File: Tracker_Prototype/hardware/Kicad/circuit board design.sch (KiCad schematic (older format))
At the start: 30 parts, among them J1 Conn_01x06, J2 GND, J3 3.3V, J4 Unconnected, U1 MAX-M8C, U3 CMWX1ZZABZ-078, U6 MS5607-02BA

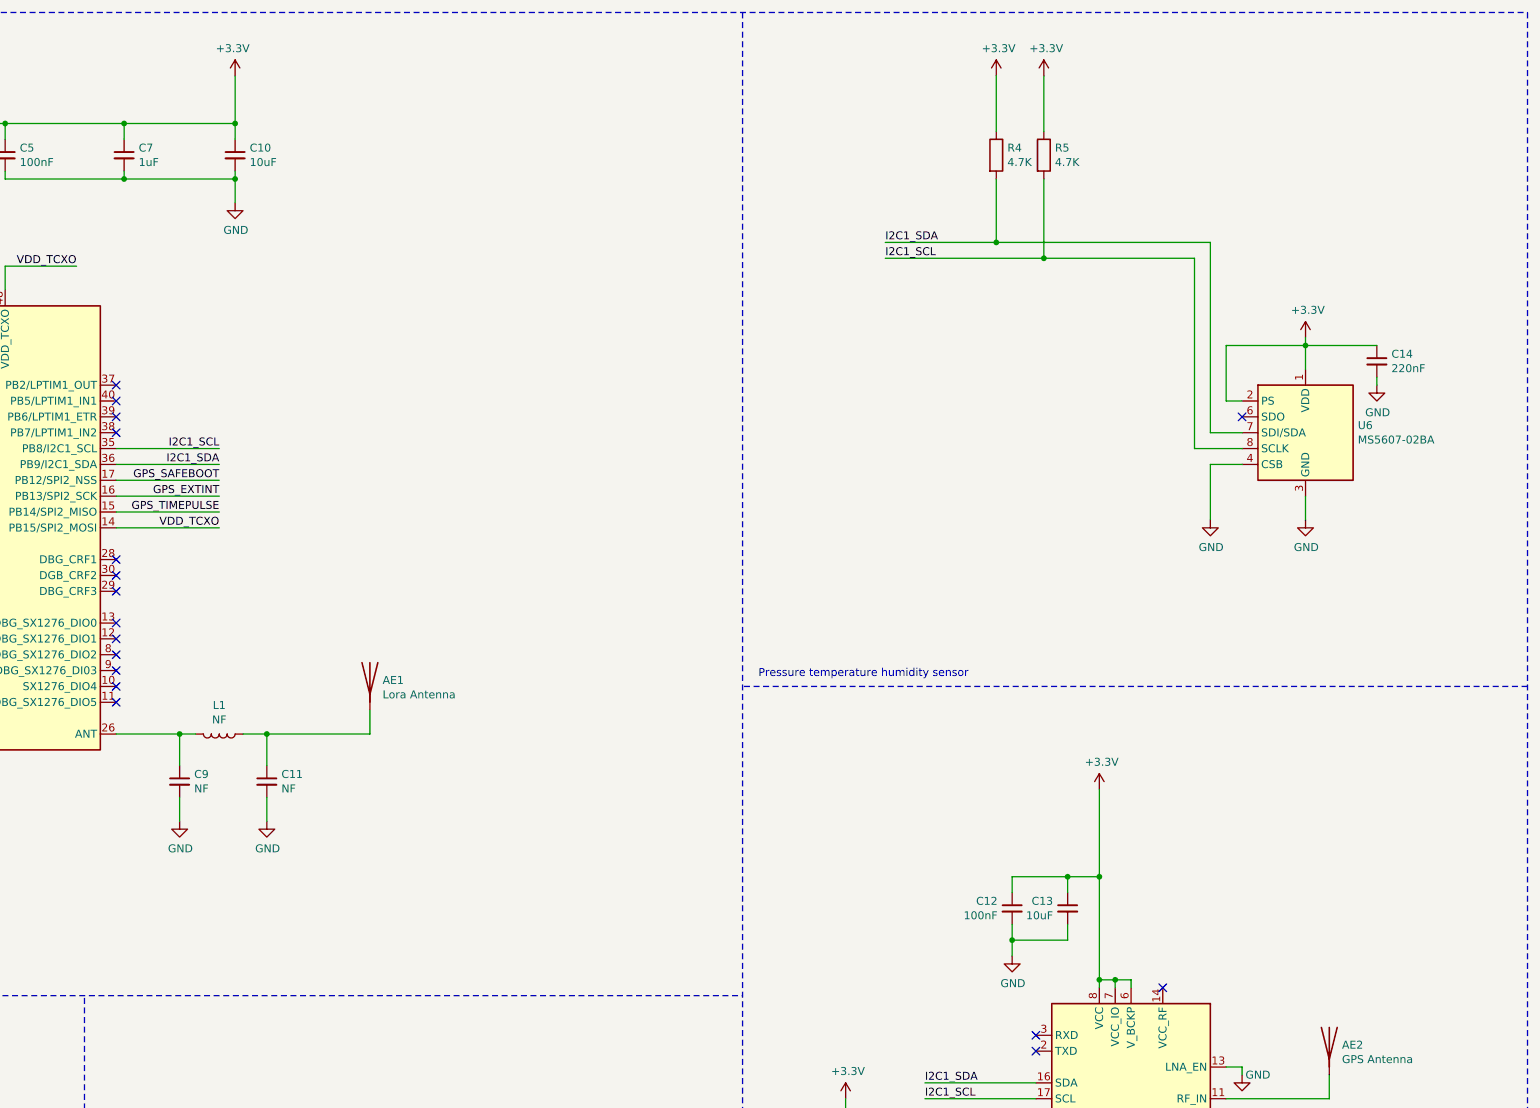
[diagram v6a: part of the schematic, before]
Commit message: added in indicator LED, added in push button to circuit only.
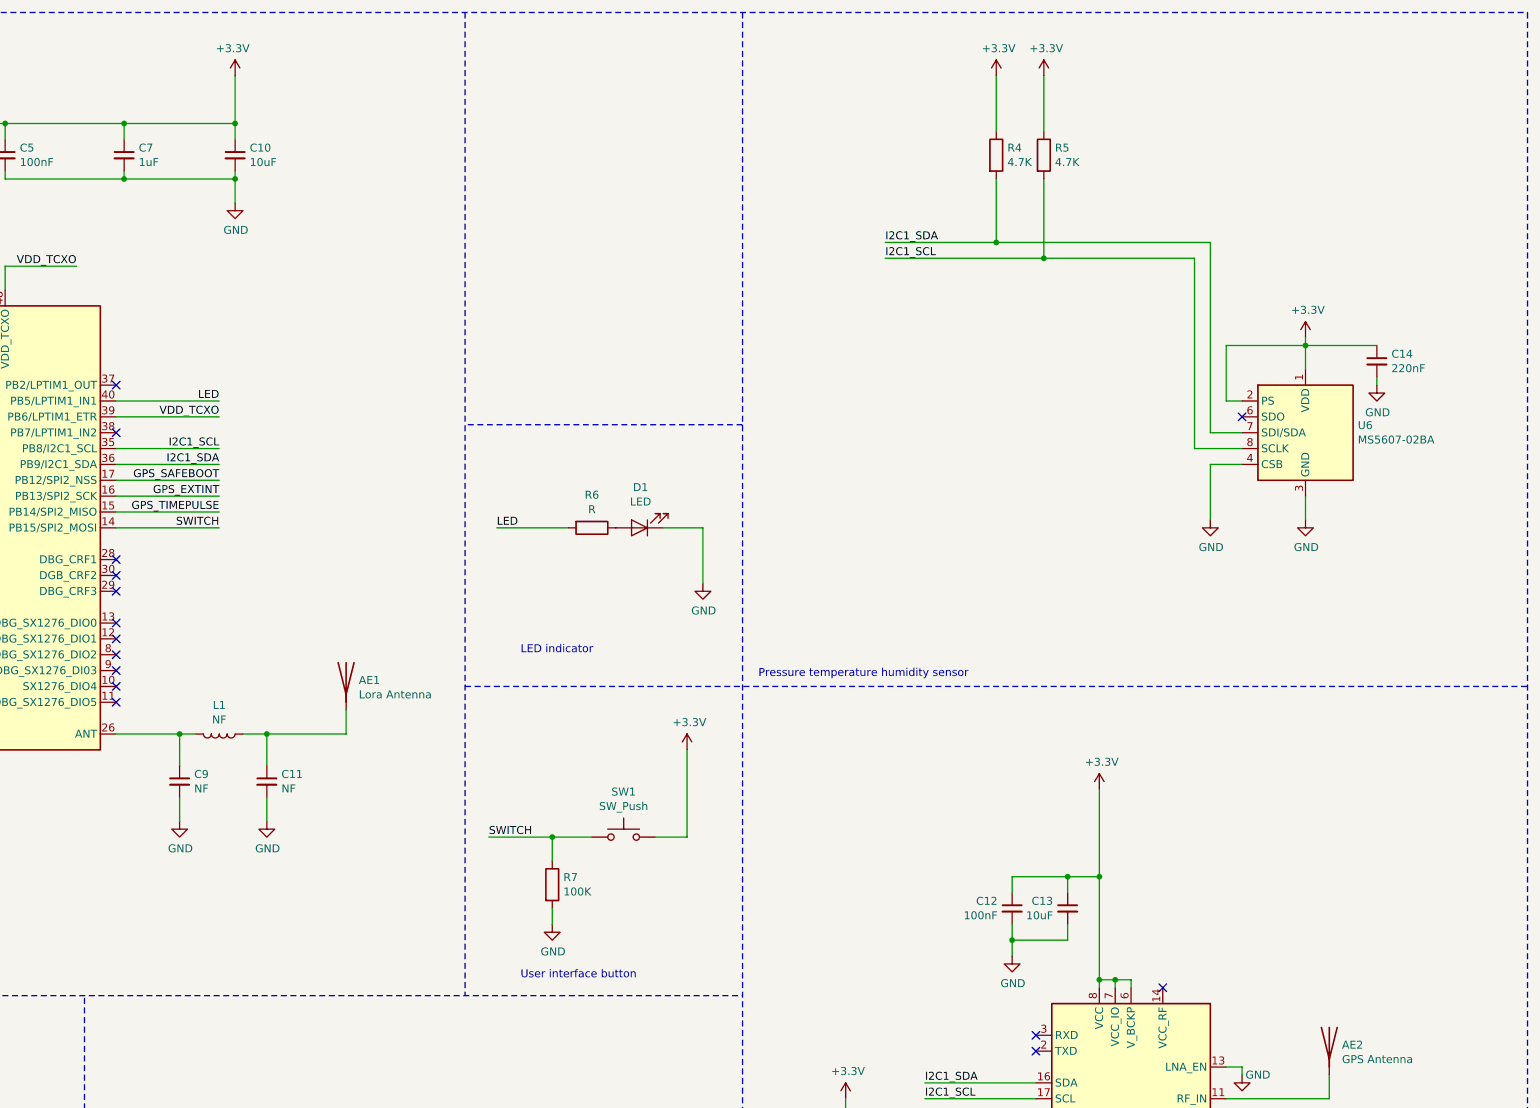
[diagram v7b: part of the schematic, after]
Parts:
- added D1: LED, LED_SMD:LED_0402_1005Metric, symbol Device:LED
- added R6: R, Resistor_SMD:R_0402_1005Metric, symbol Device:R
- added R7: 100K, Resistor_SMD:R_0402_1005Metric, symbol Device:R
- added SW1: SW_Push, symbol Switch:SW_Push
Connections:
- net +3V3: now also SW1.2
- net GND: now also D1.1 (K), R7.2
- net VDD_TCXO: now also U3.39 (PB6/LPTIM1_ETR); no longer U3.14 (PB15/SPI2_MOSI)
- net LED: now reaches U3.40 (PB5/LPTIM1_IN1)
- net LED: now also R6.2
- new net: D1.2 (A), R6.1
- new net SWITCH: R7.1, SW1.1, U3.14 (PB15/SPI2_MOSI)
- no-connect marks 33 -> 31
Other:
- note added: "LED indicator\n"
- note added: "User interface button\n"
- moved on the sheet: AE1
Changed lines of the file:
@@
 Text Notes 11200 4850 0    50   ~ 0
 Pressure temperature humidity sensor\n
-Wire Notes Line
-	16050 4900 11100 4900
 Text Notes 11200 9100 0    50   ~ 0
 GPS circuit\n
@@
 I2C1_SDA
 Wire Wire Line
-	8750 5200 8750 5050
-Wire Wire Line
-	8100 5200 8750 5200
+	8600 5200 8600 5050
+Wire Wire Line
+	8100 5200 8600 5200
 Text Label 12000 2100 0    50   ~ 0
 I2C1_SDA
@@
 GPS_EXTINT
 NoConn ~ 7150 3000
-NoConn ~ 7150 3100
-NoConn ~ 7150 3200
 NoConn ~ 7150 3300
 NoConn ~ 7150 4100
@@
 L Device:Antenna AE1
 U 1 1 5DE442FF
-P 8750 4850
-F 0 "AE1" H 8830 4839 50  0000 L CNN
-F 1 "Lora Antenna" H 8830 4748 50  0000 L CNN
-F 2 "Connector_Wire:SolderWirePad_1x01_Drill0.8mm" H 8750 4850 50  0001 C CNN
-F 3 "~" H 8750 4850 50  0001 C CNN
-	1    8750 4850
+P 8600 4850
+F 0 "AE1" H 8680 4839 50  0000 L CNN
+F 1 "Lora Antenna" H 8680 4748 50  0000 L CNN
+F 2 "Connector_Wire:SolderWirePad_1x01_Drill0.8mm" H 8600 4850 50  0001 C CNN
+F 3 "~" H 8600 4850 50  0001 C CNN
+	1    8600 4850
 	1    0    0    -1
 $EndComp
@@
 Text Label 4900 4000 0    50   ~ 0
 SWDIO
-Text Label 7800 3900 2    50   ~ 0
+Text Label 7800 3200 2    50   ~ 0
 VDD_TCXO
 Wire Wire Line
-	7150 3900 7800 3900
+	7150 3200 7800 3200
 Wire Wire Line
 	6050 1350 6050 2400
@@
 NoConn ~ 8950 7650
 NoConn ~ 5350 3900
+Wire Wire Line
+	7150 3100 7800 3100
+Wire Wire Line
+	10850 3900 10850 4250
+$Comp
+L power:GND #PWR?
+U 1 1 5DBBC44F
+P 10850 4250
+AR Path="/5D5B15F7/5DBBC44F" Ref="#PWR?"  Part="1"
+AR Path="/5DBBC44F" Ref="#PWR02"  Part="1"
+F 0 "#PWR02" H 10850 4000 50  0001 C CNN
+F 1 "GND" H 10855 4077 50  0000 C CNN
+F 2 "" H 10850 4250 50  0001 C CNN
+F 3 "" H 10850 4250 50  0001 C CNN
+	1    10850 4250
+	1    0    0    -1
+$EndComp
+$Comp
+L Device:LED D1
+U 1 1 5DBC4B62
+P 10450 3900
+F 0 "D1" H 10443 3645 50  0000 C CNN
+F 1 "LED" H 10443 3736 50  0000 C CNN
+F 2 "LED_SMD:LED_0402_1005Metric" H 10450 3900 50  0001 C CNN
+F 3 "~" H 10450 3900 50  0001 C CNN
+	1    10450 3900
+	-1   0    0    1
+$EndComp
+Wire Wire Line
+	10600 3900 10850 3900
+$Comp
+L Device:R R6
+U 1 1 5DBC5657
+P 10150 3900
+F 0 "R6" V 9943 3900 50  0000 C CNN
+F 1 "R" V 10034 3900 50  0000 C CNN
+F 2 "Resistor_SMD:R_0402_1005Metric" V 10080 3900 50  0001 C CNN
+F 3 "~" H 10150 3900 50  0001 C CNN
+	1    10150 3900
+	0    1    1    0
+$EndComp
+Wire Wire Line
+	7150 3900 7800 3900
+Text Label 7800 3900 2    50   ~ 0
+SWITCH
+Wire Notes Line
+	9350 4900 16050 4900
+Wire Wire Line
+	10150 5850 9900 5850
+Text Label 9500 5850 0    50   ~ 0
+SWITCH
+Wire Wire Line
+	9900 5850 9900 6000
+Connection ~ 9900 5850
+Wire Wire Line
+	9900 5850 9500 5850
+$Comp
+L power:GND #PWR?
+U 1 1 5DC040B5
+P 9900 6400
+AR Path="/5D5B15F7/5DC040B5" Ref="#PWR?"  Part="1"
+AR Path="/5DC040B5" Ref="#PWR03"  Part="1"
+F 0 "#PWR03" H 9900 6150 50  0001 C CNN
+F 1 "GND" H 9905 6227 50  0000 C CNN
+F 2 "" H 9900 6400 50  0001 C CNN
+F 3 "" H 9900 6400 50  0001 C CNN
+	1    9900 6400
+	1    0    0    -1
+$EndComp
+$Comp
+L Switch:SW_Push SW1
+U 1 1 5DC04C37
+P 10350 5850
+F 0 "SW1" H 10350 6135 50  0000 C CNN
+F 1 "SW_Push" H 10350 6044 50  0000 C CNN
+F 2 "" H 10350 6050 50  0001 C CNN
+F 3 "~" H 10350 6050 50  0001 C CNN
+	1    10350 5850
+	1    0    0    -1
+$EndComp
+Wire Wire Line
+	10550 5850 10750 5850
+$Comp
+L power:+3.3V #PWR?
+U 1 1 5DC0A475
+P 10750 5300
+AR Path="/5D5B165E/5DC0A475" Ref="#PWR?"  Part="1"
+AR Path="/5D5B15F7/5DC0A475" Ref="#PWR?"  Part="1"
+AR Path="/5DC0A475" Ref="#PWR04"  Part="1"
+F 0 "#PWR04" H 10750 5150 50  0001 C CNN
+F 1 "+3.3V" H 10765 5473 50  0000 C CNN
+F 2 "" H 10750 5300 50  0001 C CNN
+F 3 "" H 10750 5300 50  0001 C CNN
+	1    10750 5300
+	1    0    0    -1
+$EndComp
+$Comp
+L Device:R R7
+U 1 1 5DC0F569
+P 9900 6150
+F 0 "R7" H 9970 6196 50  0000 L CNN
+F 1 "100K" H 9970 6105 50  0000 L CNN
+F 2 "Resistor_SMD:R_0402_1005Metric" V 9830 6150 50  0001 C CNN
+F 3 "~" H 9900 6150 50  0001 C CNN
+	1    9900 6150
+	1    0    0    -1
+$EndComp
+Text Notes 9700 6750 0    50   ~ 0
+User interface button\n
+Wire Wire Line
+	9900 6300 9900 6400
+Wire Wire Line
+	10750 5300 10750 5850
+Wire Notes Line
+	9350 650  9350 6850
+Text Label 7800 3100 2    50   ~ 0
+LED
+Text Label 9550 3900 0    50   ~ 0
+LED
+Wire Wire Line
+	10000 3900 9550 3900
+Wire Notes Line
+	11100 3250 9350 3250
+Text Notes 9700 4700 0    50   ~ 0
+LED indicator\n
 $EndSCHEMATC
